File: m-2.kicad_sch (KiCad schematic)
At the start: 27 parts, among them J2 Bus_M.2_1-2199230-6, M3 Mech_M2_2280_H2.5mm, Y1 Oscillator_32.768kHz_ECS_2520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

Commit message: Schematic Cleanup, Complete routing
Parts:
- removed M3: Mech_M2_2280_H2.5mm, JetsonCarrier:Mech_M2_2280_H2.5mm, symbol antmicroModules:Mech_M2_2280_H2.5mm
- C13, C14, C15, C16, C17, C18, C20: value C_220n_0402 -> 220nF; symbol antmicroCapacitors0402:C_220n_0402 -> Device:C_Small
- C19: value C_220n_0402 -> 220nF; symbol antmicroCapacitors0402:C_220n_0402 -> Device:C_Small; Val 220n -> 220nF
- C21, C23, C24: value C_10u_0603 -> 10uF; symbol antmicroCapacitors0603:C_10u_0603 -> Device:C_Small
- C22: value C_10u_0603 -> 10uF; symbol antmicroCapacitors0603:C_10u_0603 -> Device:C_Small; Val 10u -> 10uF
- C25: value C_100n_0603 -> 100nF; symbol antmicroCapacitors0402:C_100n_0402 -> Device:C_Small
- D1: symbol antmicroLEDIndicationDiscrete:LED_G_0603_LTST-C190GKT -> Device:LED_Small_Filled
- H5: renamed from SP8; value Spacer_H2.5mm_9774025151 -> 9774025151; symbol antmicroMechanicalParts:Spacer_Drill3.7mm_H2.5mm_9774025151R -> Mechanical:MountingHole_Pad; now left out of the parts list
- J2: value Bus_M.2_1-2199230-6 -> 1-2199230-6; symbol antmicroPciConnectors:Bus_M.2_1-2199230-6 -> JetsonCarrier:Bus_M.2_1-2199230-6
- R13, R19: value R_0R_0402 -> 0R; symbol antmicroResistors0402:R_0R_0402 -> Device:R_Small
- R143: value R_0R_22.4A_0603 -> 0R; symbol antmicroResistors0603:R_0R_22.4A_0603 -> Device:R_Small
- R37, R38: value R_47k_0402 -> 47k; symbol antmicroResistors0402:R_47k_0402 -> Device:R_Small; now in the parts list
- R39: value R_200R_0603 -> 3K3; symbol antmicroResistors0402:R_200R_0402 -> Device:R_Small; MPN CR0402-FX-2000GLF -> (none); Val 200R -> 3K3
- TP10, TP11, TP12: symbol antmicroTestPoints:TP_0.75mm_SMD -> Connector:TestPoint
- Y1: value Oscillator_32.768kHz_ECS_2520MV -> ECS-327MVATX-2-CN-TR3; symbol antmicroOscillators:Oscillator_32.768kHz_ECS_2520MV -> JetsonCarrier:ECS_2520MV
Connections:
- net +3V3: now also C25.2, R143.1, R39.1; no longer C25.1, R143.2, R39.2
- net 32.7KHZ_OUT: now also R19.2; no longer R19.1
- net 3V3_M2: now also R143.2; no longer R143.1
- net C_PCIE0_TX0_N: now also C17.2; no longer C17.1
- net C_PCIE0_TX0_P: now also C13.2; no longer C13.1
- net GND: now also C25.1; no longer C25.2
- net M2_M_SUSCLK: now also R19.1; no longer R19.2
- net PCIE0_TX0_N: now also C17.1; no longer C17.2
- net PCIE0_TX0_P: now also C13.1; no longer C13.2
- net at D1.2 (A): now also R39.2; no longer R39.1
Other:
- moved on the sheet: C13, C14, C15, C16, C17, C18, C19, C20, C21, C22, C23, C24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

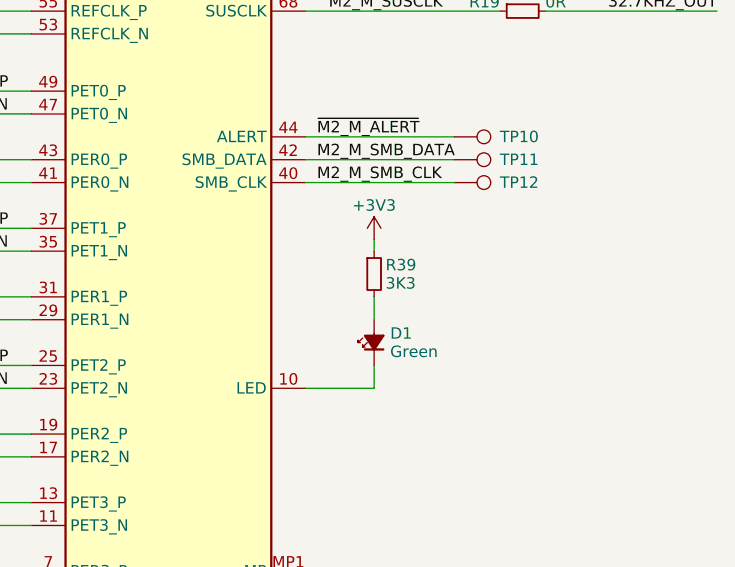
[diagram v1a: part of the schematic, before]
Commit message: Complete Silkscreen
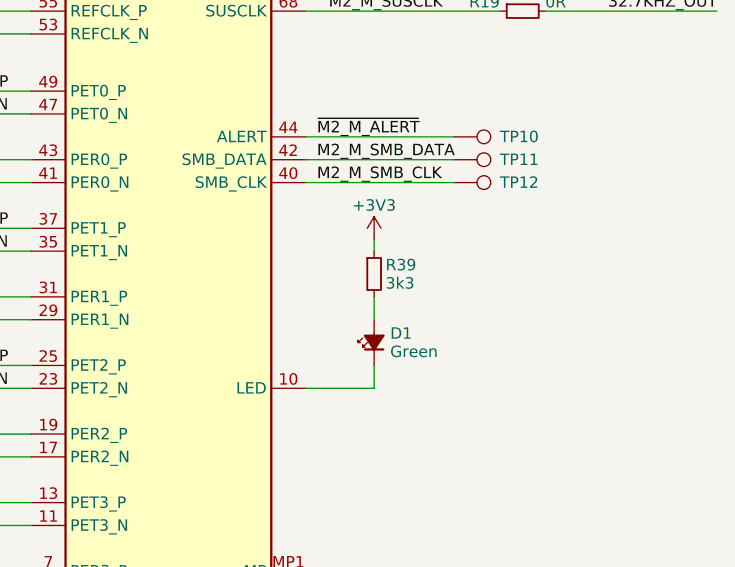
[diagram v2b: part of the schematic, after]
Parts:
- R39: value 3K3 -> 3k3
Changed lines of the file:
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@@
 	(title_block
 		(title "Jetson Carrier Board")
-		(date "2024-07-05")
+		(date "2024-07-10")
 		(rev "v1")
 		(company "Argus-1 Cubesat")
@@
 			)
 		)
-		(property "Value" "3K3"
+		(property "Value" "3k3"
 			(at 237.49 140.208 0)
 			(effects
